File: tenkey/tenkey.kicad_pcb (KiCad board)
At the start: 2 copper layers, 78.7 x 97.8 mm, 53 parts, among them J1 USB, P1 SCK, P2 MISO, P3 MOSI, P4 RESET, P5 5V, P6 GND, SW0:0 NUM_0, SW0:2 DOT, SW1 RESET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

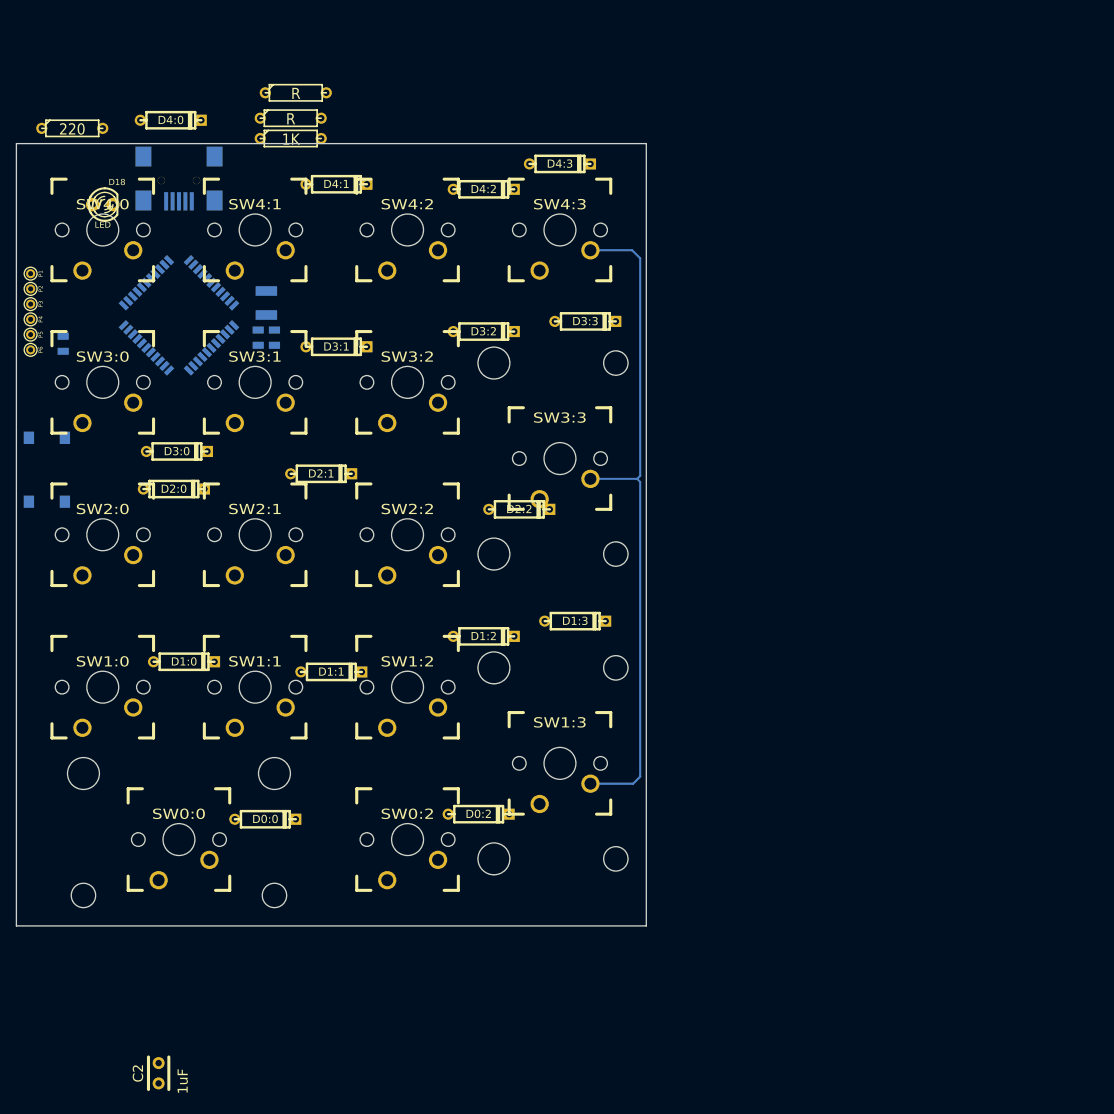
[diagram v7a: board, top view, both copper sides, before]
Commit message: somehow managed to get most everything routed with only 1 jumper (and possibly 1 more)
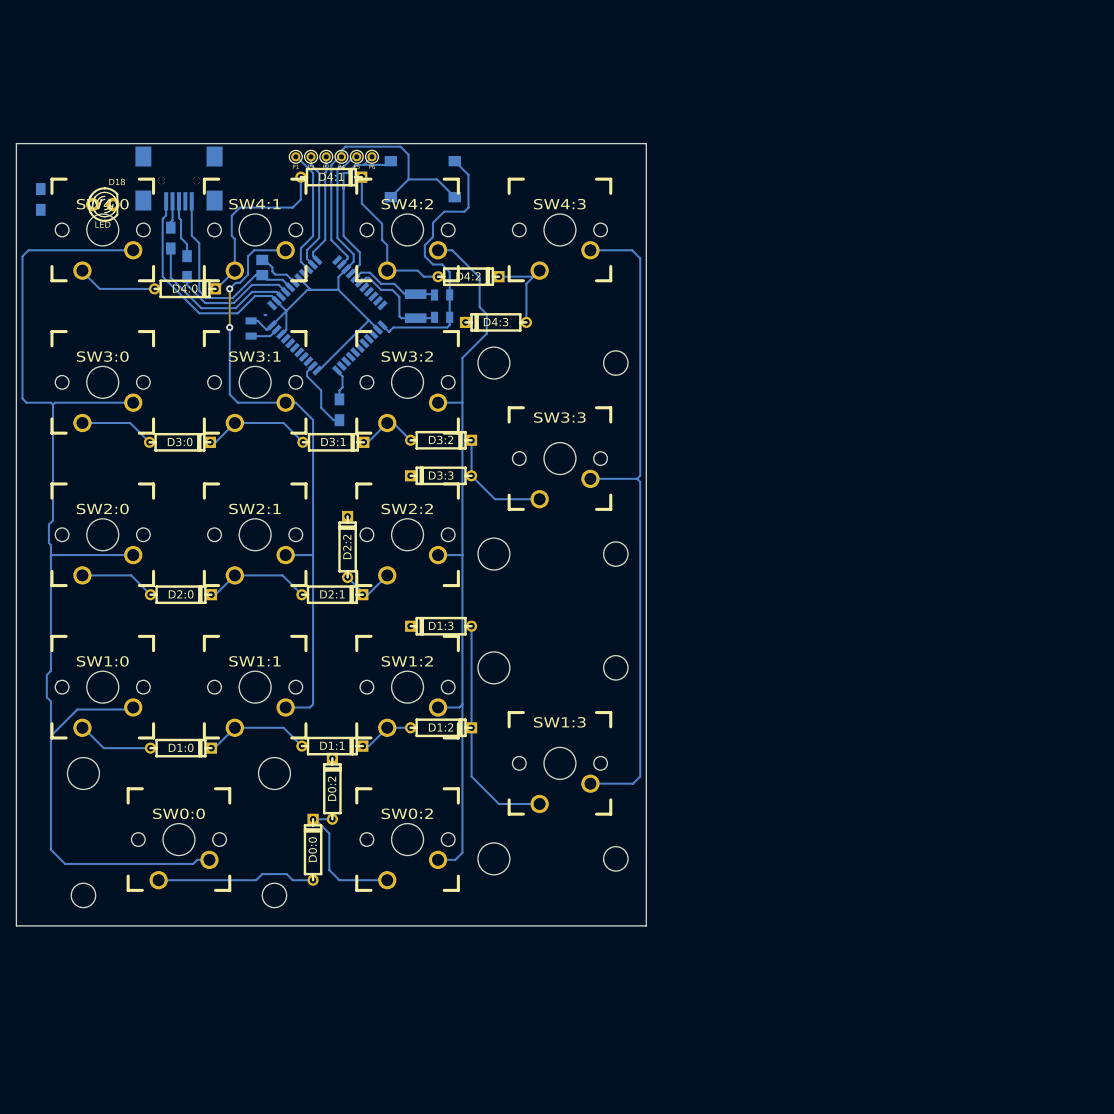
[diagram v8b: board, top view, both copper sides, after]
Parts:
- C2: footprint Capacitors_ThroughHole:Capacitor4x3RM2.5 -> Capacitors_SMD:c_0805; moved to B.Cu
- R1, R5: footprint Discret:R3 -> Resistors_SMD:Resistor_SMD0805_HandSoldering; moved to B.Cu
- R3, R4: value R -> 22; footprint Discret:R3 -> Resistors_SMD:Resistor_SMD0805_HandSoldering; moved to B.Cu
- X1: value CRYSTAL -> 16 MHz
- moved C2 102.8 mm to (131.1, 75.8)
- moved SW1 59.4 mm to (151.1, 64.8), turned to 180 degrees
- moved P6 49.0 mm to (144.8, 62.0), turned to 180 degrees
- moved P5 46.4 mm to (142.9, 62.0), turned to 180 degrees
- moved P4 43.9 mm to (141.0, 62.0), turned to 180 degrees
- moved P2 40.5 mm to (139.1, 62.0), turned to 180 degrees
- moved P3 39.6 mm to (137.2, 62.0), turned to 180 degrees
- moved P1 36.2 mm to (135.3, 62.0), turned to 180 degrees
- moved R5 34.5 mm to (140.7, 93.6), turned to 90 degrees
- moved D3:3 26.4 mm to (153.4, 101.9), turned to 180 degrees
- moved R3 24.0 mm to (119.6, 72.1), turned to 90 degrees
- moved C1 23.6 mm to (129.7, 83.4)
- moved C3 23.1 mm to (153.5, 82.0), turned to 0 degrees
- moved R4 22.6 mm to (121.7, 75.7), turned to 90 degrees
- moved D2:2 22.0 mm to (141.7, 110.7), turned to 90 degrees
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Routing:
- net /COL0: track 0.00 -> 146.4 mm
- net GND: track 0.00 -> 95.6 mm
- net /COL2: track 0.00 -> 92.9 mm
- net /+5V: track 0.00 -> 87.0 mm
- net /COL1: track 0.00 -> 79.1 mm, vias 0 -> 2
- net /RESET: track 0.00 -> 38.0 mm
- net Net-(D1:2-Pad2): track 0.00 -> 28.7 mm
- net Net-(D4:0-Pad2): track 0.00 -> 22.6 mm
- net Net-(R3-Pad1): track 0.00 -> 20.1 mm
- net Net-(D0:0-Pad1): track 0.00 -> 19.9 mm
- net Net-(D4:1-Pad2): track 0.00 -> 19.7 mm
- net Net-(D0:0-Pad2): track 0.00 -> 17.5 mm
- net /SCK: track 0.00 -> 16.0 mm
- net Net-(R4-Pad1): track 0.00 -> 15.6 mm
- net /MOSI: track 0.00 -> 14.9 mm
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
